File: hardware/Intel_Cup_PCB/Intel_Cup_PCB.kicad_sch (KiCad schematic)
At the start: 27 parts, among them U1 DRV8833PW

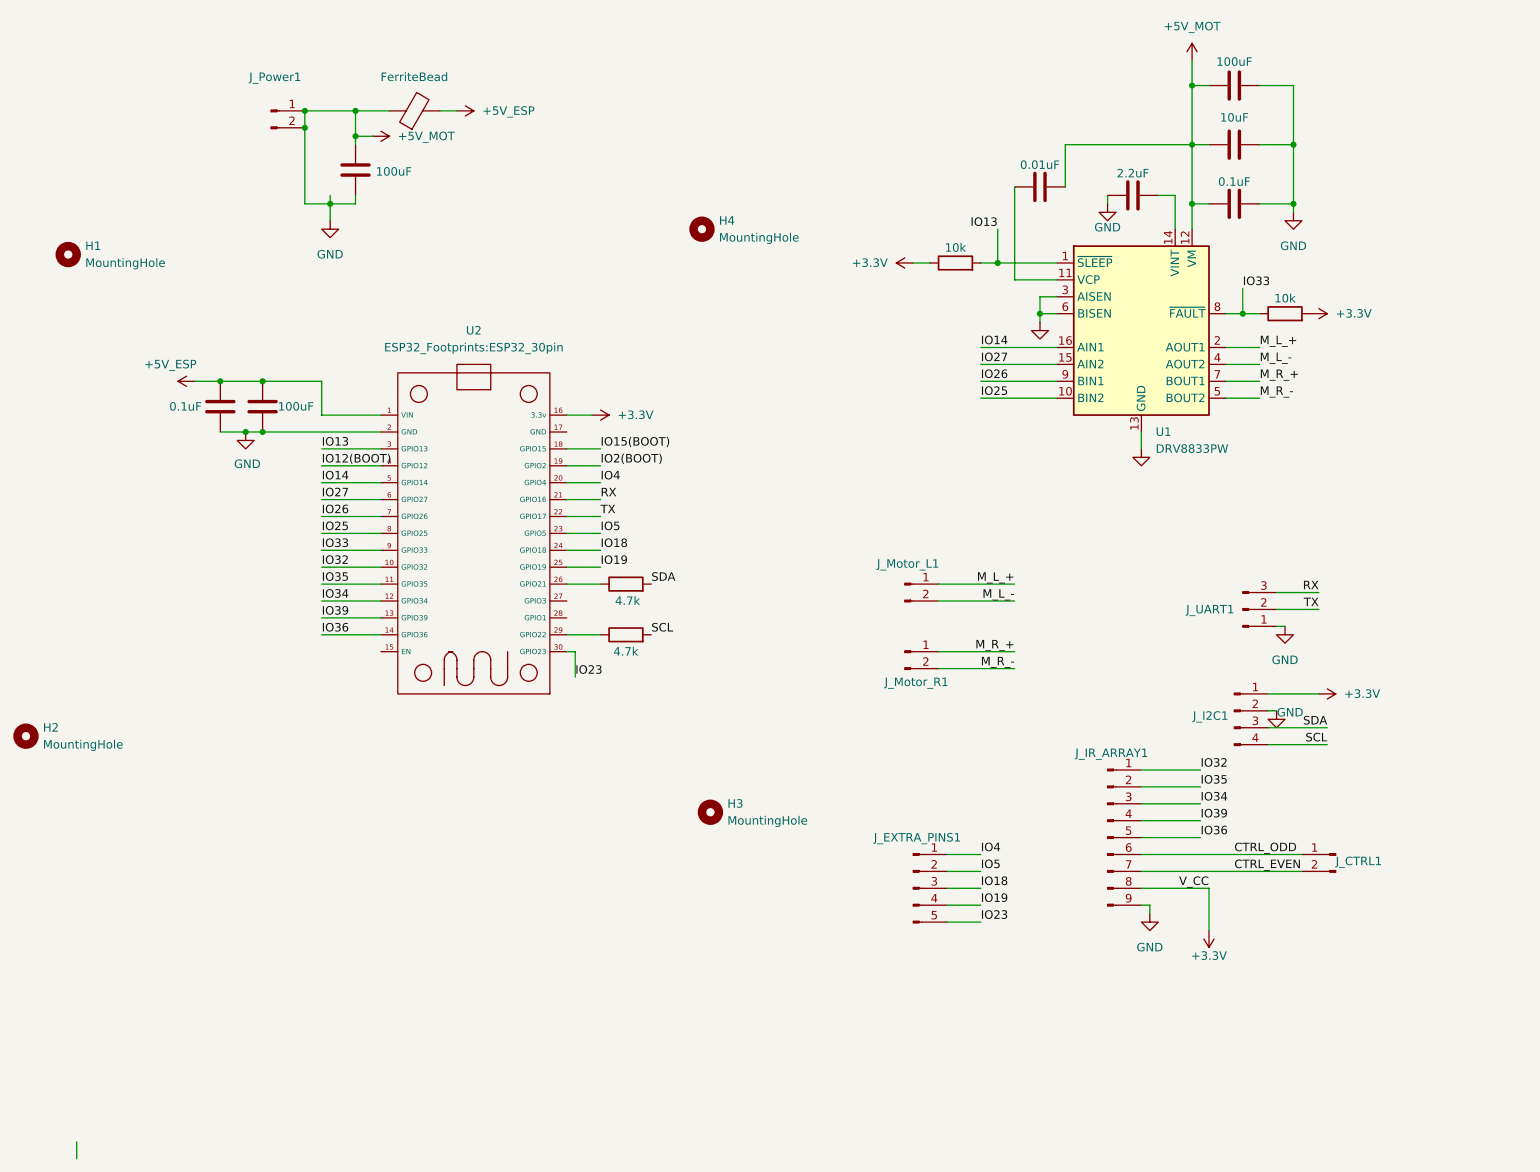
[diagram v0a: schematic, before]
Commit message: Added footprints for all components(might still need changing) and started PCB placement
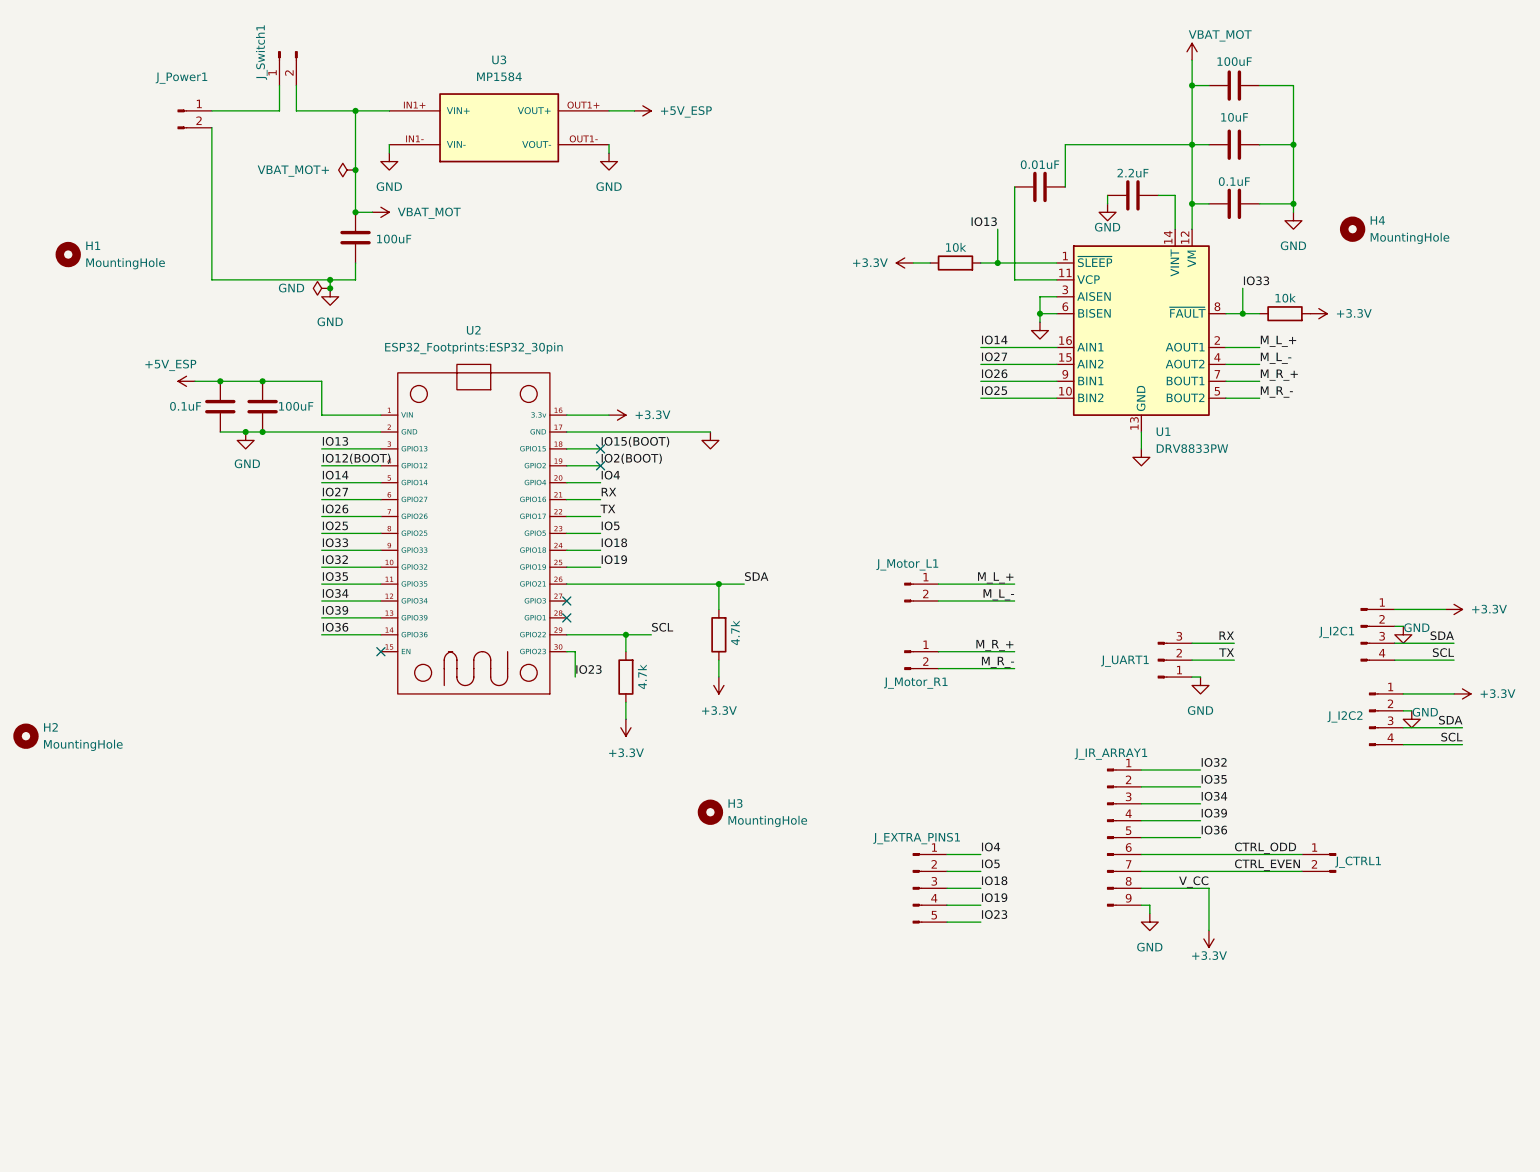
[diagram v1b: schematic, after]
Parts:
- removed FB1: FerriteBead, symbol Device:FerriteBead
- added J_I2C2: (no value), Connector_PinSocket_2.54mm:PinSocket_1x04_P2.54mm_Vertical, symbol Connector:Conn_01x04_Pin
- added J_Switch1: Conn_01x02_Pin, TerminalBlock_RND:TerminalBlock_RND_205-00012_1x02_P5.00mm_Horizontal, symbol Connector:Conn_01x02_Pin
- added U3: MP1584, MP1584_Footprint:DC-BRICK, symbol MP1584:MP1584
- C1, C3, C4, C5, C8: footprint (none) -> Capacitor_SMD:C_0805_2012Metric_Pad1.18x1.45mm_HandSolder
- C2, C6, C7: footprint (none) -> Capacitor_THT:CP_Radial_D6.3mm_P2.50mm
- H1, H2, H3, H4: footprint (none) -> MountingHole:MountingHole_3.2mm_M3
- J_EXTRA_PINS1: footprint (none) -> Connector_PinSocket_2.54mm:PinSocket_1x05_P2.54mm_Vertical
- J_I2C1: footprint (none) -> Connector_PinSocket_2.54mm:PinSocket_1x04_P2.54mm_Vertical
- J_IR_ARRAY1: footprint (none) -> Connector_PinHeader_2.54mm:PinHeader_1x09_P2.54mm_Vertical
- J_Motor_L1: footprint Connector_JST:JST_EH_B2B-EH-A_1x02_P2.50mm_Vertical -> TerminalBlock_RND:TerminalBlock_RND_205-00012_1x02_P5.00mm_Horizontal
- J_Motor_R1, J_Power1: footprint (none) -> TerminalBlock_RND:TerminalBlock_RND_205-00012_1x02_P5.00mm_Horizontal
- J_UART1: footprint (none) -> Connector_PinSocket_2.54mm:PinSocket_1x03_P2.54mm_Vertical
- R3, R4: footprint (none) -> Resistor_SMD:R_0805_2012Metric_Pad1.20x1.40mm_HandSolder
- R_SCL_Pullup_DNP1: renamed from R2; footprint (none) -> Resistor_SMD:R_0805_2012Metric_Pad1.20x1.40mm_HandSolder
- R_SDA_Pullup_DNP1: renamed from R1; footprint (none) -> Resistor_SMD:R_0805_2012Metric_Pad1.20x1.40mm_HandSolder
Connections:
- net +3.3V: now also R_SCL_Pullup_DNP1.1, R_SDA_Pullup_DNP1.1, J_I2C2.1 (Pin_1)
- net +5V_ESP: now also U3.OUT1+ (VOUT+), U3.OUT2+ (VOUT+)
- net SCL: now also U2.29 (GPIO22), J_I2C2.4 (Pin_4)
- net SDA: now also U2.26 (GPIO21), J_I2C2.3 (Pin_3)
- net GND: now reaches U2.17 (GND)
- net GND: now also C1.2, C2.1, C3.2, C4.2, C6.2, C7.1, C8.1, J_I2C1.2 (Pin_2), J_IR_ARRAY1.9 (Pin_9), J_Power1.2 (Pin_2), J_UART1.1 (Pin_1), U1.13 (GND), U1.3 (AISEN), U1.6 (BISEN), U2.2 (GND), J_I2C2.2 (Pin_2), U3.IN1- (VIN-), U3.IN2- (VIN-), U3.OUT1- (VOUT-), U3.OUT2- (VOUT-)
- removed net +5V_MOT: C1.1, C1.2, C2.1, C2.2, C3.1, C3.2, C4.2, C5.2, C6.1, C6.2, C7.1, C8.1, J_I2C1.2 (Pin_2), J_IR_ARRAY1.9 (Pin_9), J_Power1.1 (Pin_1), J_Power1.2 (Pin_2), J_UART1.1 (Pin_1), U1.12 (VM), U1.13 (GND), U1.3 (AISEN), U1.6 (BISEN), U2.2 (GND)
- new net: J_Power1.1 (Pin_1), J_Switch1.1 (Pin_1)
- new net VBAT_MOT: C1.1, C2.2, C3.1, C5.2, C6.1, J_Switch1.2 (Pin_2), U1.12 (VM), U3.IN1+ (VIN+), U3.IN2+ (VIN+)
- no-connect marks 0 -> 5
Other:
- moved on the sheet: H4, J_I2C1, J_Power1, J_UART1

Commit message: Placement before routing
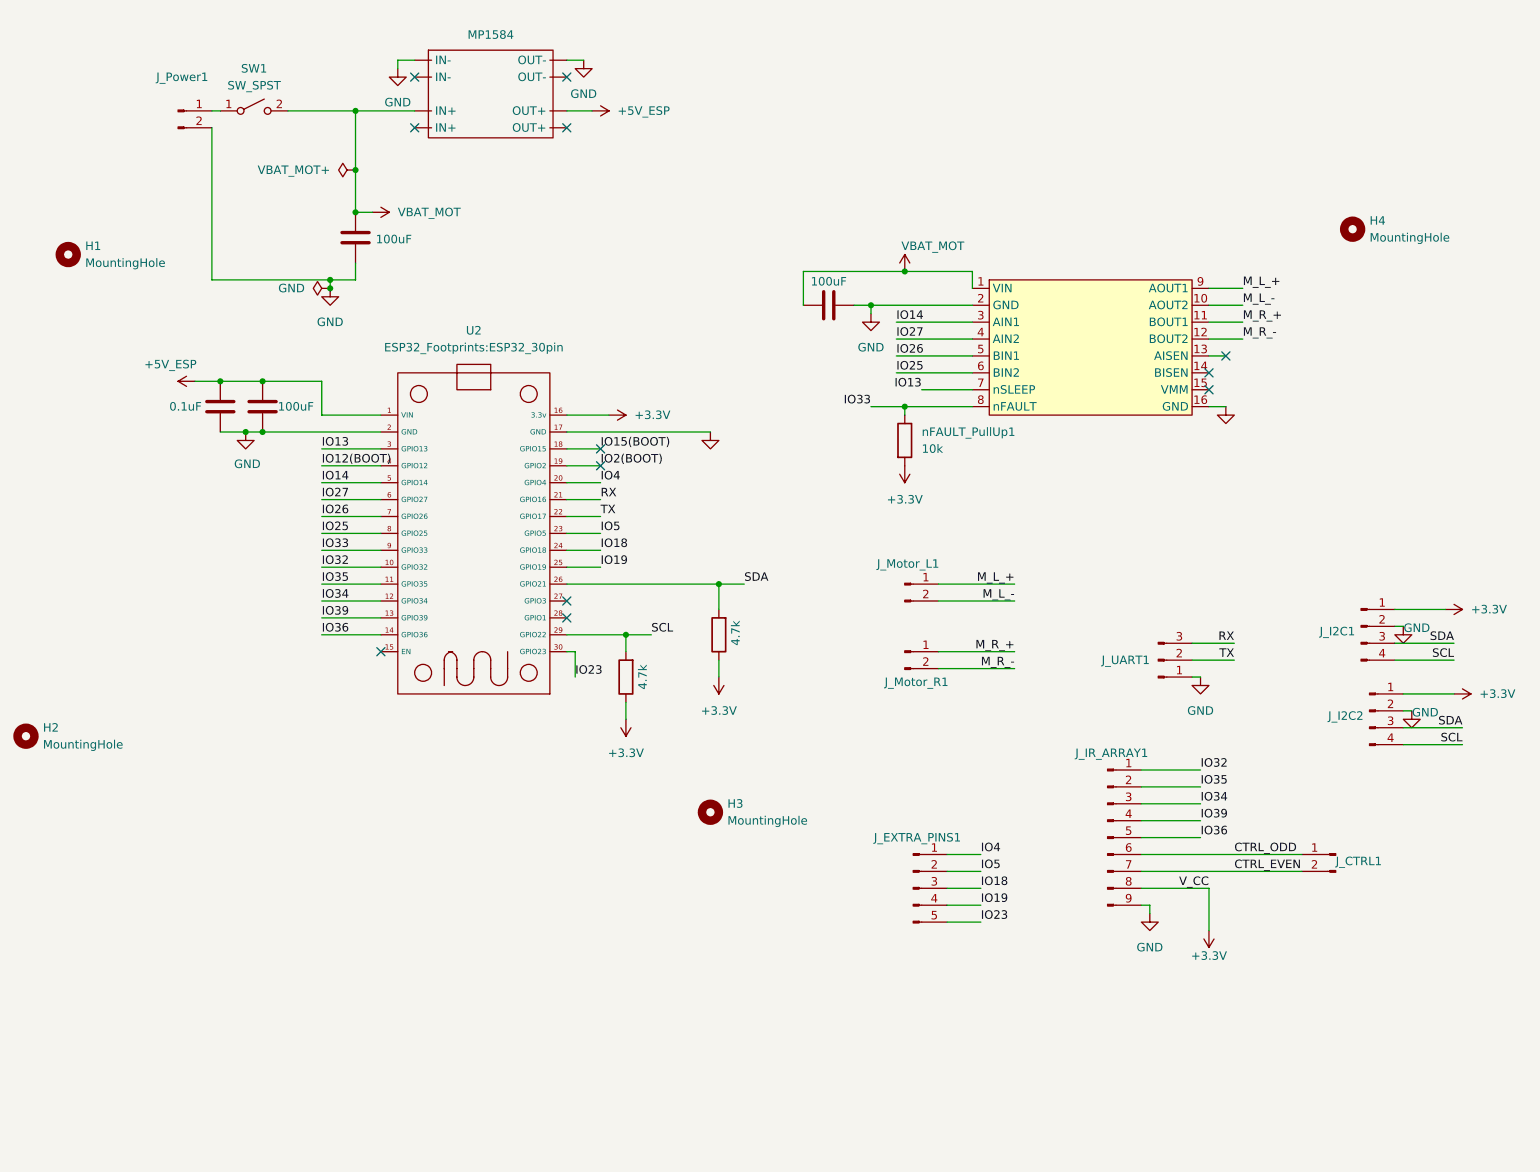
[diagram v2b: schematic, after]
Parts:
- removed C1: 0.1uF, Capacitor_SMD:C_0805_2012Metric_Pad1.18x1.45mm_HandSolder, symbol Device:C
- removed C3: 10uF, Capacitor_SMD:C_0805_2012Metric_Pad1.18x1.45mm_HandSolder, symbol Device:C
- removed C4: 2.2uF, Capacitor_SMD:C_0805_2012Metric_Pad1.18x1.45mm_HandSolder, symbol Device:C
- removed C5: 0.01uF, Capacitor_SMD:C_0805_2012Metric_Pad1.18x1.45mm_HandSolder, symbol Device:C
- removed J_Switch1: Conn_01x02_Pin, TerminalBlock_RND:TerminalBlock_RND_205-00012_1x02_P5.00mm_Horizontal, symbol Connector:Conn_01x02_Pin
- removed R3, R4: 10k, Resistor_SMD:R_0805_2012Metric_Pad1.20x1.40mm_HandSolder, symbol Device:R
- removed U1: DRV8833PW, Package_SO:TSSOP-16_4.4x5mm_P0.65mm, symbol Driver_Motor:DRV8833PW
- removed U3: MP1584, MP1584_Footprint:DC-BRICK, symbol MP1584:MP1584
- added MP1584: (no value), intel_cup_footprints:Untitled, symbol Memory_Flash:MP1584_Breakout
- added SW1: SW_SPST, Button_Switch_SMD:SW_DIP_SPSTx01_Slide_9.78x4.72mm_W8.61mm_P2.54mm, symbol Switch:SW_SPST
- added U5: (no value), intel_cup_footprints:Polulu_DRV8833, symbol Memory_Flash:DRV_8833_Pololu_Breakout
- added nFAULT_PullUp1: 10k, symbol Device:R
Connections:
- net +3.3V: now also nFAULT_PullUp1.2
- net +5V_ESP: now also MP1584. (OUT+)
- net GND: now also MP1584. (OUT+), U5.16 (GND), U5.2 (GND)
- net IO13: now also U5.7 (nSLEEP)
- net IO14: now also U5.3 (AIN1)
- net IO25: now also U5.6 (BIN2)
- net IO26: now also U5.5 (BIN1)
- net IO27: now also U5.4 (AIN2)
- net IO33: now also U5.8 (nFAULT), nFAULT_PullUp1.1
- net M_L_+: now also U5.9 (AOUT1)
- net M_L_-: now also U5.10 (AOUT2)
- net M_R_+: now also U5.11 (BOUT1)
- net M_R_-: now also U5.12 (BOUT2)
- net VBAT_MOT: now also MP1584. (OUT+), SW1.2 (B), U5.1 (VIN)
- net at J_Power1.1 (Pin_1): now also SW1.1 (A)
- no-connect marks 5 -> 12

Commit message: Added new nets for MP1584 and fixed footprints
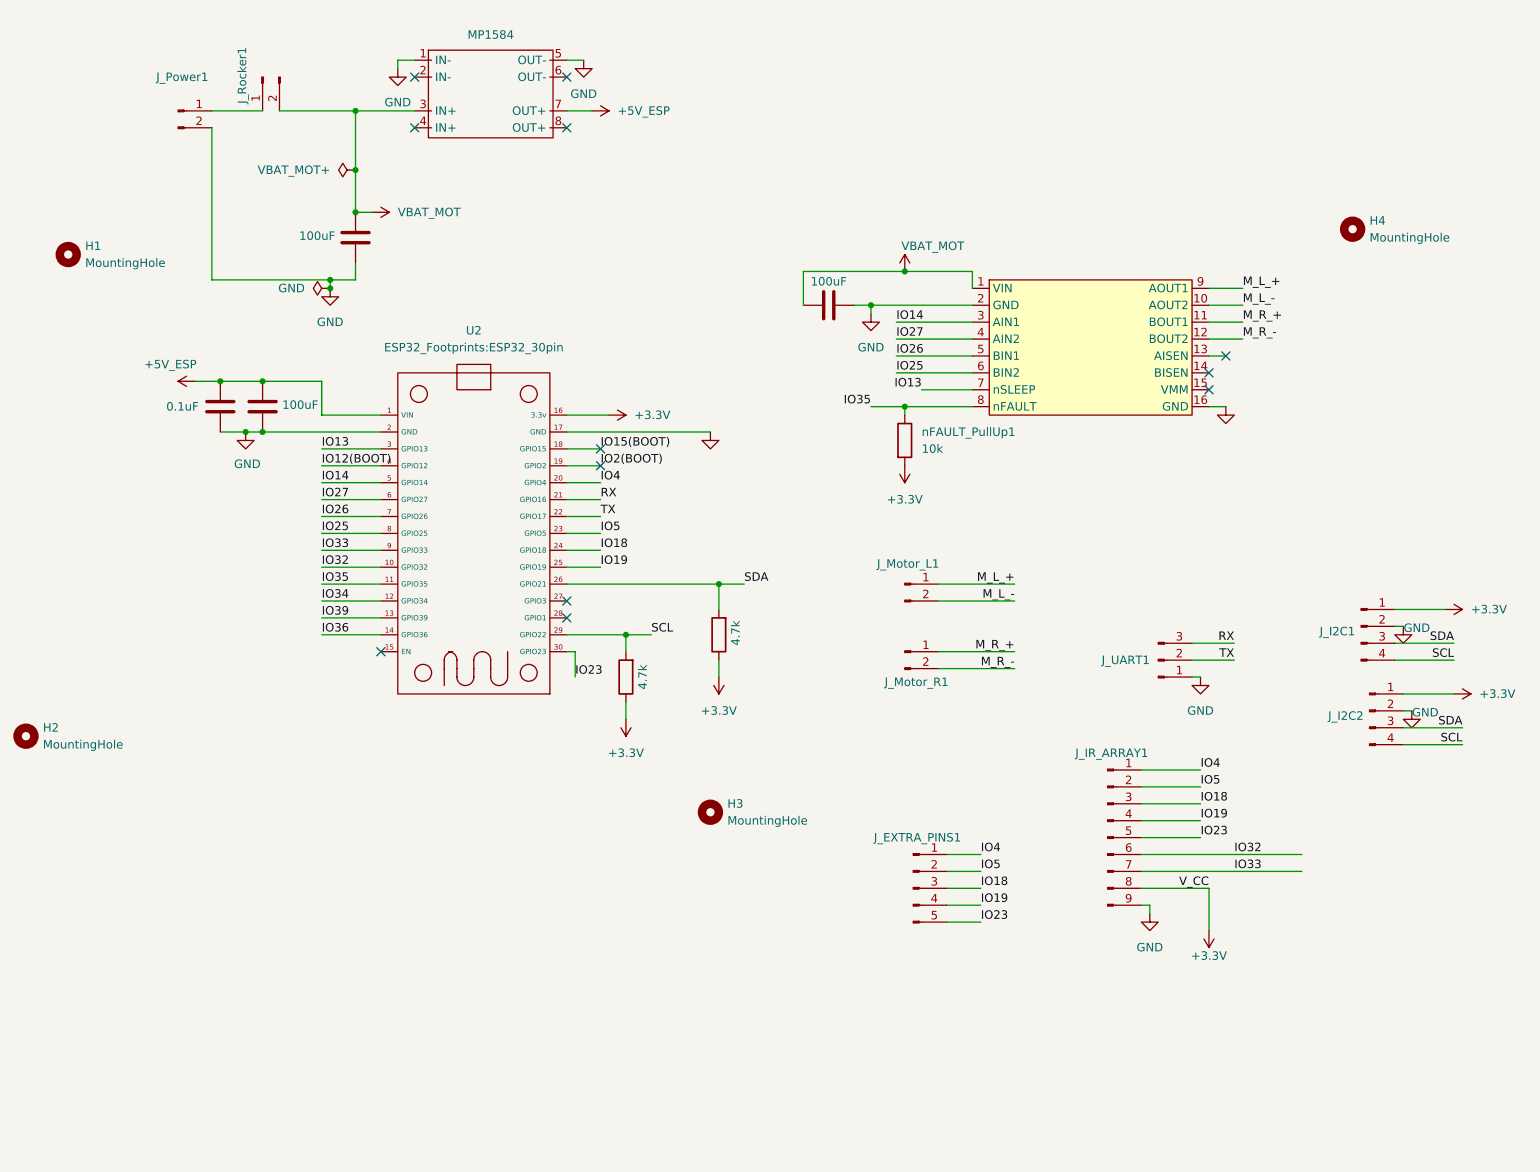
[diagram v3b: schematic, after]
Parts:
- removed J_CTRL1: (no value), symbol Connector:Conn_01x02_Pin
- removed SW1: SW_SPST, Button_Switch_SMD:SW_DIP_SPSTx01_Slide_9.78x4.72mm_W8.61mm_P2.54mm, symbol Switch:SW_SPST
- added J_Rocker1: Conn_01x02_Pin, TerminalBlock_RND:TerminalBlock_RND_205-00012_1x02_P5.00mm_Horizontal, symbol Connector:Conn_01x02_Pin
- C8: footprint Capacitor_SMD:C_0805_2012Metric_Pad1.18x1.45mm_HandSolder -> Capacitor_THT:C_Disc_D3.0mm_W1.6mm_P2.50mm
- R_SCL_Pullup_DNP1, R_SDA_Pullup_DNP1: footprint Resistor_SMD:R_0805_2012Metric_Pad1.20x1.40mm_HandSolder -> Resistor_THT:R_Axial_DIN0207_L6.3mm_D2.5mm_P7.62mm_Horizontal
- nFAULT_PullUp1: footprint (none) -> Resistor_THT:R_Axial_DIN0207_L6.3mm_D2.5mm_P7.62mm_Horizontal
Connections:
- net CTRL_EVEN is gone; now on net IO33: J_IR_ARRAY1.7 (Pin_7)
- net CTRL_ODD is gone; now on net IO32: J_IR_ARRAY1.6 (Pin_6)
- net +5V_ESP: now also C7.1, C8.1, MP1584.7 (OUT+); no longer C7.2, C8.2, MP1584. (OUT+)
- net GND: now also C2.2, C7.2, C8.2, MP1584.1 (IN-), MP1584.5 (OUT-); no longer C2.1, C7.1, C8.1, MP1584. (OUT+)
- net IO18: now also J_IR_ARRAY1.3 (Pin_3)
- net IO19: now also J_IR_ARRAY1.4 (Pin_4)
- net IO23: now also J_IR_ARRAY1.5 (Pin_5)
- net IO32: no longer J_IR_ARRAY1.1 (Pin_1)
- net IO33: no longer U5.8 (nFAULT), nFAULT_PullUp1.1
- net IO34: no longer J_IR_ARRAY1.3 (Pin_3)
- net IO35: now also U5.8 (nFAULT), nFAULT_PullUp1.1; no longer J_IR_ARRAY1.2 (Pin_2)
- net IO36: no longer J_IR_ARRAY1.5 (Pin_5)
- net IO39: no longer J_IR_ARRAY1.4 (Pin_4)
- net IO4: now also J_IR_ARRAY1.1 (Pin_1)
- net IO5: now also J_IR_ARRAY1.2 (Pin_2)
- net VBAT_MOT: now also C2.1, MP1584.3 (IN+), J_Rocker1.2 (Pin_2); no longer C2.2, MP1584. (OUT+)
- net at J_Power1.1 (Pin_1): now also J_Rocker1.1 (Pin_1)

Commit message: Minor fixes
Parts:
- MP1584: value (none) -> MP1584
- renumbered U2 to ESP32_Devkit1
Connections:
- net IO12(BOOT): now also J_EXTRA_PINS1.4 (Pin_4)
- net IO15(BOOT): now also J_EXTRA_PINS1.5 (Pin_5)
- net IO18: no longer J_EXTRA_PINS1.3 (Pin_3)
- net IO19: no longer J_EXTRA_PINS1.4 (Pin_4)
- net IO23: no longer J_EXTRA_PINS1.5 (Pin_5)
- net IO34: now also J_EXTRA_PINS1.1 (Pin_1)
- net IO36: now also J_EXTRA_PINS1.2 (Pin_2)
- net IO39: now also J_EXTRA_PINS1.3 (Pin_3)
- net IO4: no longer J_EXTRA_PINS1.1 (Pin_1)
- net IO5: no longer J_EXTRA_PINS1.2 (Pin_2)
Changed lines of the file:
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@@
 		)
 	)
-	(label "IO4"
+	(label "IO34"
 		(at 203.2 148.59 0)
 		(effects
@@
 		)
 	)
-	(label "IO19"
+	(label "IO12(BOOT)"
 		(at 203.2 156.21 0)
 		(effects
@@
 		)
 	)
-	(label "IO23"
+	(label "IO15(BOOT)"
 		(at 203.2 158.75 0)
 		(effects
@@
 		)
 	)
-	(label "IO18"
+	(label "IO39"
 		(at 203.2 153.67 0)
 		(effects
@@
 		)
 	)
-	(label "IO5"
+	(label "IO36"
 		(at 203.2 151.13 0)
 		(effects
@@
 			)
 		)
-		(property "Value" ""
+		(property "Value" "MP1584"
 			(at 129.54 34.29 0)
 			(show_name no)
@@
 		(in_pos_files yes)
 		(dnp no)
-		(property "Reference" "U2"
+		(property "Reference" "ESP32_Devkit1"
 			(at 127 69.85 90)
 			(show_name no)
@@
 			(project "Intel_Cup_PCB"
 				(path "/3fe6b950-a1b3-4d6d-b01d-5b57f82620e1"
-					(reference "U2")
+					(reference "ESP32_Devkit1")
 					(unit 1)
 				)
